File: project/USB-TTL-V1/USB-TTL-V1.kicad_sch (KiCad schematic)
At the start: 22 parts, among them J1 TTL, J2 usbc, Q1 q1, Q2 q2, U1 CH340C, U2 SPX3819M5-L-3-3

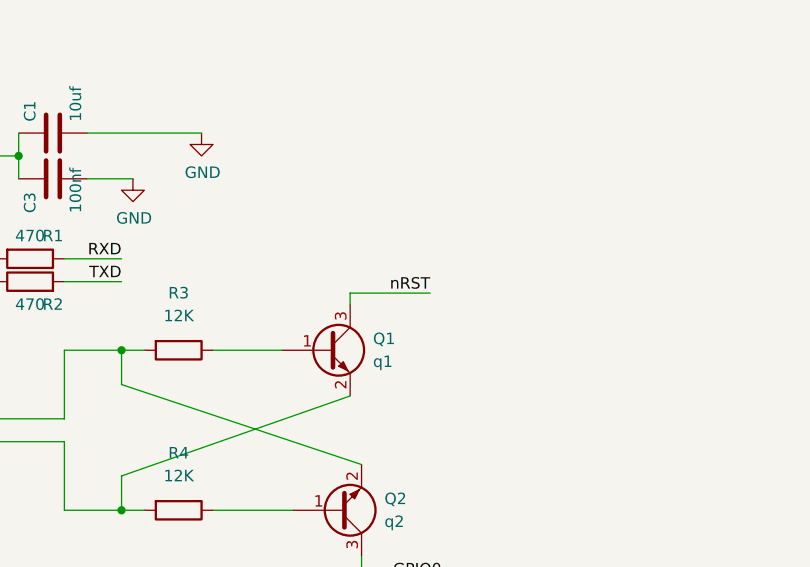
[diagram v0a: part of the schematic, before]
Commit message: fix: screen rst and cs
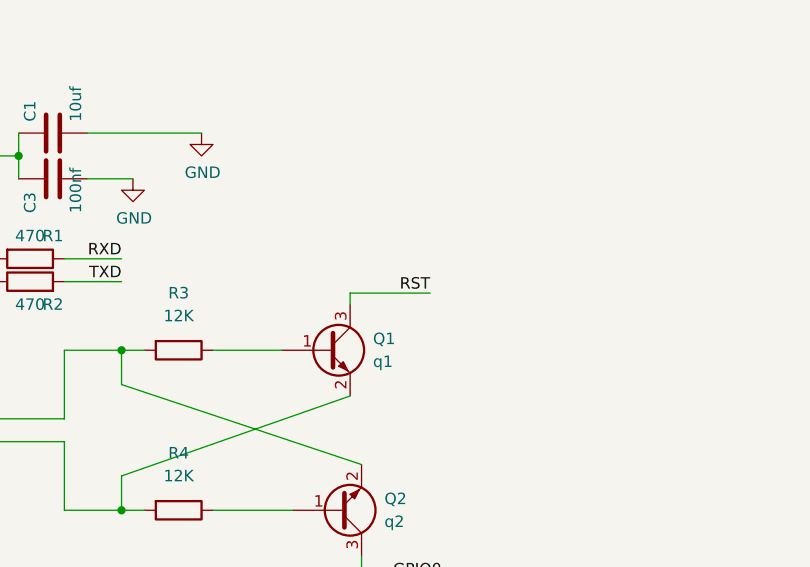
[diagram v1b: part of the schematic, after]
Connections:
- net nRST is gone; now on net RST: Q1.3 (C)
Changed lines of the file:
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@@
     (effects (font (size 4 4) (thickness 0.8) bold) (justify left bottom))
   )
-  (label "nRST" (at 162.56 80.645 180)
+  (label "RST" (at 162.56 80.645 180)
     (effects (font (size 1.27 1.27)) (justify right bottom))
   )
@@
   (symbol (lib_id "power:PWR_FLAG") (at 101.6 102.235 90) (unit 1)
     (in_bom yes) (on_board yes) (fields_autoplaced)
-    (property "Reference" "#FLG03" (id 0) (at 99.695 102.235 0)
+    (property "Reference" "#FLG02" (id 0) (at 99.695 102.235 0)
       (effects (font (size 1.27 1.27)) hide)
     )
@@
     )
     (path "/3b49870e-47e1-4887-b360-7eb0723c5606"
-      (reference "#FLG03") (unit 1) (value "PWR_FLAG") (footprint "")
+      (reference "#FLG02") (unit 1) (value "PWR_FLAG") (footprint "")
     )
     (path "/01c05c7f-9a74-4acc-95cb-f339df8cb185"

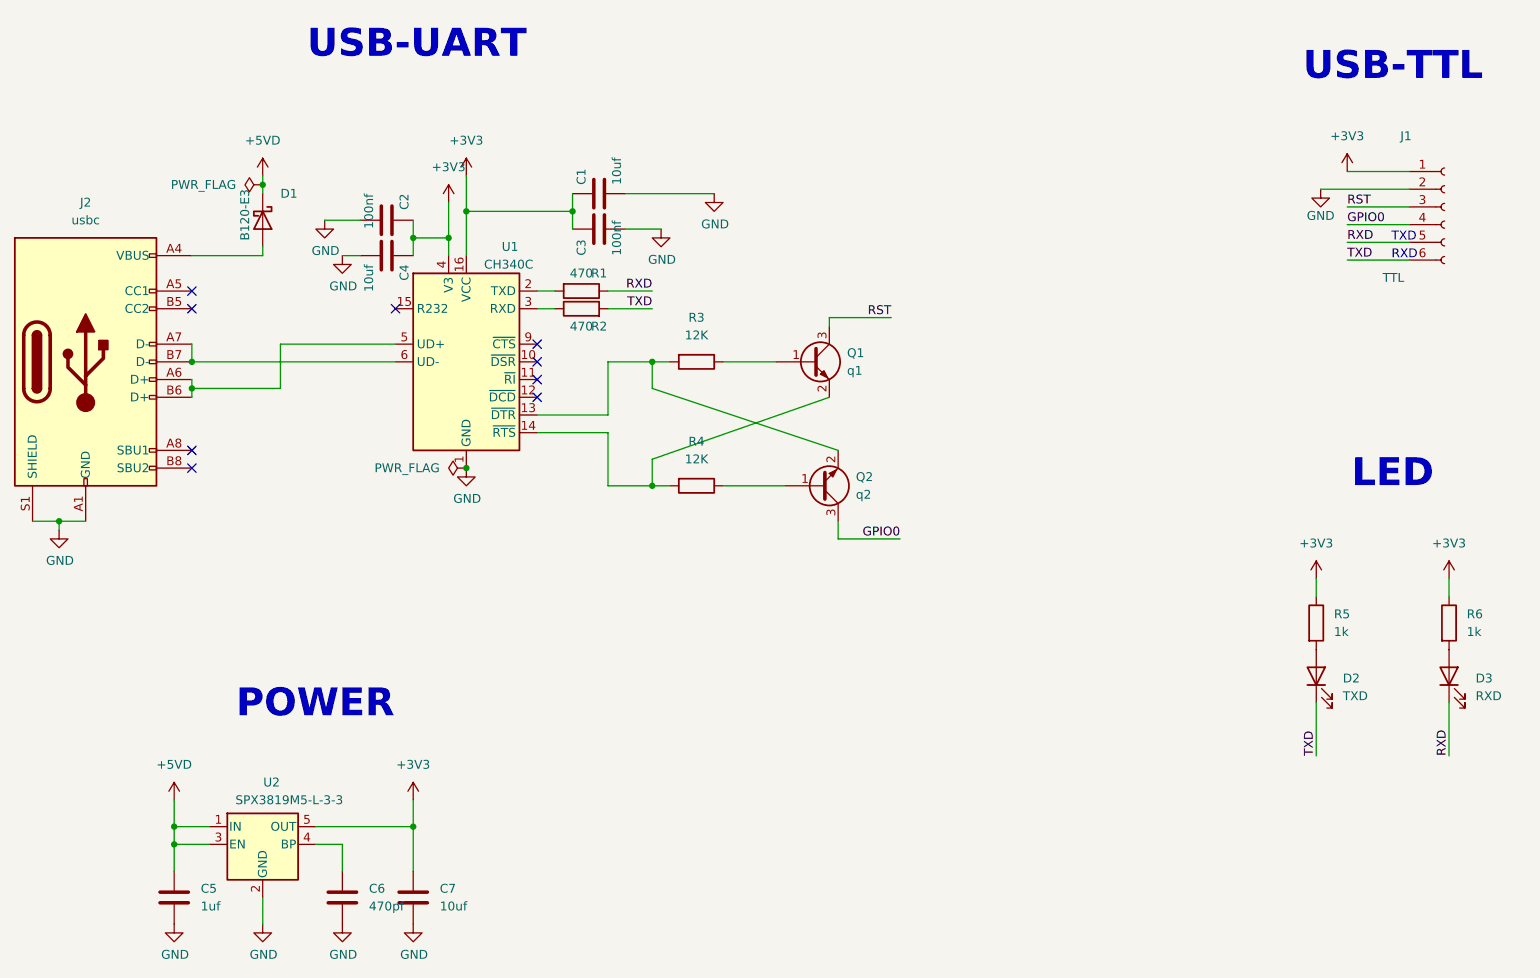
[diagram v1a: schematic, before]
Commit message: feat: update usb - ttl
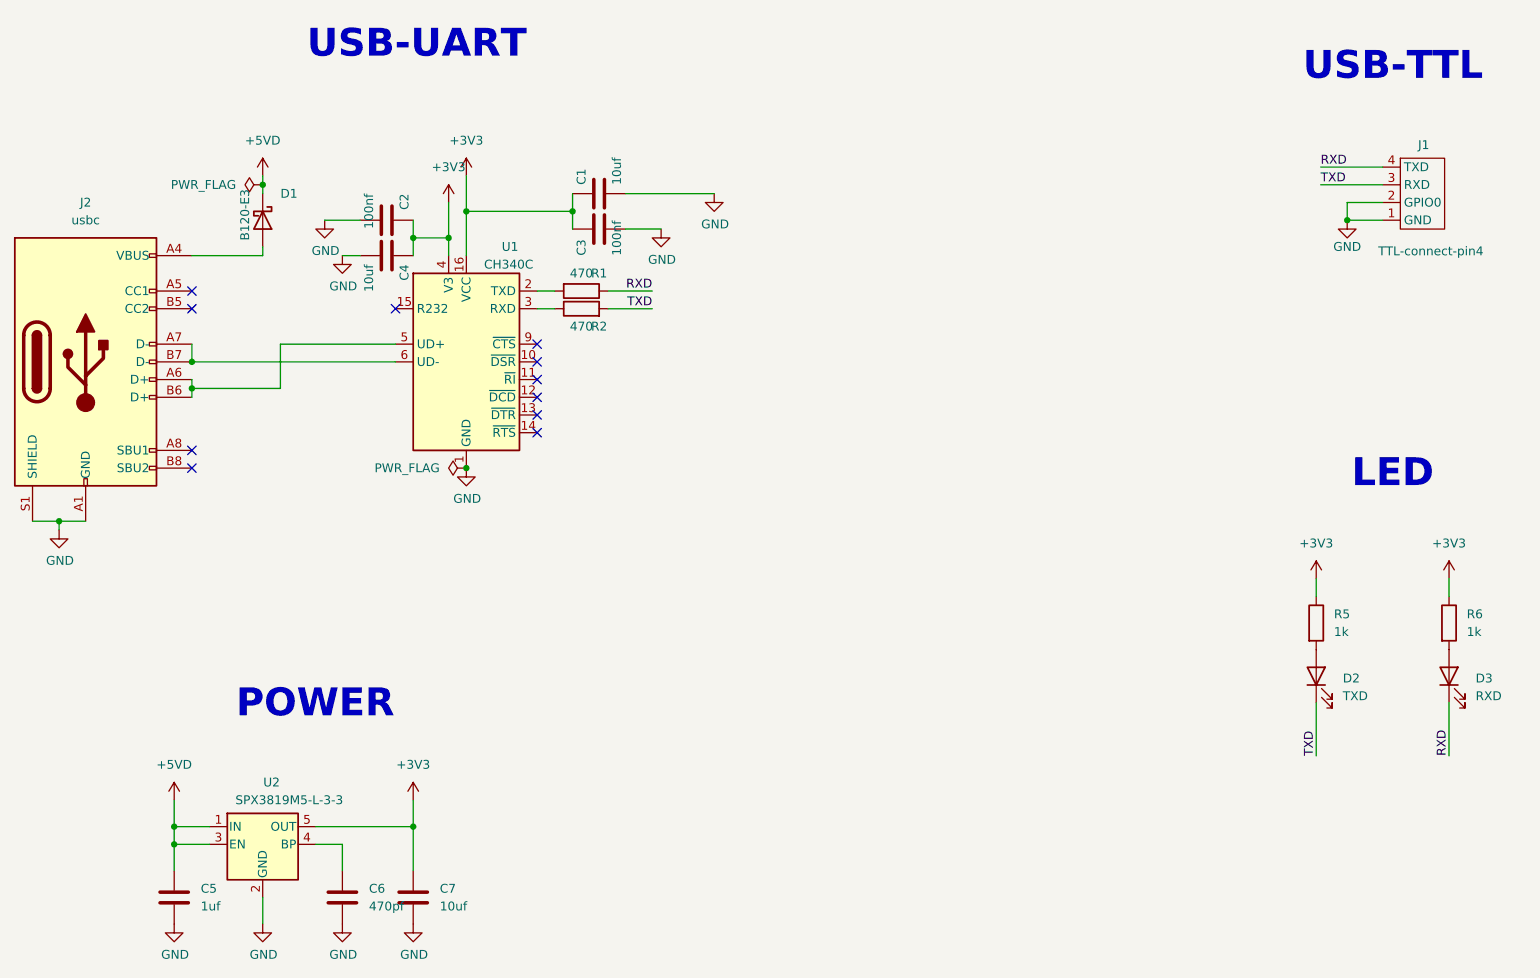
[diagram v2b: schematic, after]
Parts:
- removed J1: TTL, Connector_PinHeader_1.27mm:PinHeader_1x06_P1.27mm_Vertical, symbol Connector:Conn_01x06_Female
- removed Q1: q1, Package_TO_SOT_SMD:TSOT-23, symbol Device:Q_NPN_BEC
- removed Q2: q2, Package_TO_SOT_SMD:TSOT-23, symbol Device:Q_NPN_BEC
- removed R3, R4: 12K, Resistor_SMD:R_0402_1005Metric, symbol Device:R
- added J1: TTL-connect-pin4, Connector_PinHeader_1.27mm:PinHeader_1x04_P1.27mm_Vertical, symbol My-lib:TTL-connect-pin4
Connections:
- net GND: now also J1.1 (GND), J1.2 (GPIO0)
- net RXD: now also J1.4 (TXD)
- net TXD: now also J1.3 (RXD)
- no-connect marks 9 -> 11
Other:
- note removed: "RXD"
- note removed: "TXD"

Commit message: fix: update screen  usb-ttl
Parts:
- removed C4, C7: 10uf, Capacitor_SMD:C_0402_1005Metric, symbol Device:C
- removed C5: 1uf, Capacitor_SMD:C_0402_1005Metric, symbol Device:C
- removed C6: 470pf, Capacitor_SMD:C_0402_1005Metric, symbol Device:C
- removed D1: B120-E3, Diode_SMD:D_SOD-123, symbol Diode:B120-E3
- removed U2: SPX3819M5-L-3-3, Package_TO_SOT_SMD:SOT-23-5, symbol Regulator_Linear:SPX3819M5-L-3-3
- added Q1, Q2: S8050, Package_TO_SOT_SMD:TSOT-23, symbol Device:Q_NPN_BEC
- added R3, R4: 12K, Resistor_SMD:R_0402_1005Metric, symbol Device:R
- J1: footprint Connector_PinHeader_1.27mm:PinHeader_1x04_P1.27mm_Vertical -> Connector_PinHeader_2.00mm:PinHeader_1x05_P2.00mm_Vertical
- R5, R6: value 1k -> 4.7k
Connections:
- net GND: no longer J1.2 (GPIO0)
- net RXD: now also J1.3 (RXD); no longer J1.4 (TXD)
- net TXD: now also J1.4 (TXD); no longer J1.3 (RXD)
- net +5V: now reaches J2.A4 (VBUS), J2.A9 (VBUS), J2.B4 (VBUS), J2.B9 (VBUS)
- net +5V: now also C1.1, C2.1, R5.1, R6.1, U1.16 (VCC)
- net at U1.13 (~{DTR}): now also Q2.2 (E), R3.2
- net at U1.14 (~{RTS}): now also Q1.2 (E), R4.2
- removed net +3V3: C1.1, C2.1, C3.1, R5.1, R6.1, U1.16 (VCC), U1.4 (V3)
- new net: C3.1, U1.4 (V3)
- new net: Q2.1 (B), R4.1
- new net: Q1.1 (B), R3.1
- new net EN: J1.5 (RST), Q1.3 (C)
- new net GPIO0: J1.2 (GPIO0), Q2.3 (C)
- no-connect marks 11 -> 9
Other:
- note removed: "POWER"

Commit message: update
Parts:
- removed R1, R2: 470, Resistor_SMD:R_0402_1005Metric, symbol Device:R
- R5, R6: value 4.7k -> 12K
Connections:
- net RXD: now also U1.2 (TXD)
- net TXD: now also U1.3 (RXD)
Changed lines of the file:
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@@
     (stroke (width 0) (type default) (color 0 0 0 0))
   )
-  (wire (pts (xy 127.635 69.85) (xy 133.985 69.85))
+  (wire (pts (xy 117.475 69.85) (xy 126.365 69.85))
     (stroke (width 0) (type default) (color 0 0 0 0))
   )
@@
     (stroke (width 0) (type default) (color 0 0 0 0))
   )
-  (wire (pts (xy 117.475 72.39) (xy 120.015 72.39))
-    (stroke (width 0) (type default) (color 0 0 0 0))
-  )
   (wire (pts (xy 142.875 55.88) (xy 130.175 55.88))
     (stroke (width 0) (type default) (color 0 0 0 0))
@@
     (stroke (width 0) (type default) (color 0 0 0 0))
   )
-  (wire (pts (xy 127.635 72.39) (xy 133.985 72.39))
+  (wire (pts (xy 117.475 72.39) (xy 126.365 72.39))
     (stroke (width 0) (type default) (color 0 0 0 0))
   )
@@
   )
   (wire (pts (xy 76.2 80.01) (xy 76.2 72.39))
-    (stroke (width 0) (type default) (color 0 0 0 0))
-  )
-  (wire (pts (xy 117.475 69.85) (xy 120.015 69.85))
     (stroke (width 0) (type default) (color 0 0 0 0))
   )
@@
     (effects (font (size 1.27 1.27)) (justify left bottom))
   )
-  (label "TXD" (at 133.985 72.39 180)
+  (label "TXD" (at 126.365 72.39 180)
     (effects (font (size 1.27 1.27)) (justify right bottom))
   )
@@
     (effects (font (size 1.27 1.27)) (justify right bottom))
   )
-  (label "RXD" (at 133.985 69.85 180)
+  (label "RXD" (at 126.365 69.85 180)
     (effects (font (size 1.27 1.27)) (justify right bottom))
   )
@@
     )
     (pin "1")
-  )
-  (symbol (lib_id "Device:R") (at 123.825 69.85 270) (unit 1)
-    (in_bom yes) (on_board yes)
-    (property "Reference" "R1" (id 0) (at 128.27 67.31 90))
-    (property "Value" "470" (id 1) (at 123.825 67.31 90))
-    (property "Footprint" "Resistor_SMD:R_0402_1005Metric" (id 2) (at 123.825 68.072 90)
-      (effects (font (size 1.27 1.27)) hide)
-    )
-    (property "Datasheet" "~" (id 3) (at 123.825 69.85 0)
-      (effects (font (size 1.27 1.27)) hide)
-    )
-    (pin "1")
-    (pin "2")
   )
   (symbol (lib_id "Device:LED") (at 223.52 132.08 90) (unit 1)
@@
       (effects (font (size 1.27 1.27)) (justify left))
     )
-    (property "Value" "4.7k" (id 1) (at 245.11 125.7299 0)
+    (property "Value" "12K" (id 1) (at 245.11 125.7299 0)
       (effects (font (size 1.27 1.27)) (justify left))
     )
@@
       (effects (font (size 1.27 1.27)) (justify left))
     )
-    (property "Value" "4.7k" (id 1) (at 226.06 125.7299 0)
+    (property "Value" "12K" (id 1) (at 226.06 125.7299 0)
       (effects (font (size 1.27 1.27)) (justify left))
     )
@@
     (pin "1")
   )
-  (symbol (lib_id "Device:R") (at 123.825 72.39 90) (unit 1)
-    (in_bom yes) (on_board yes)
-    (property "Reference" "R2" (id 0) (at 128.27 74.93 90))
-    (property "Value" "470" (id 1) (at 123.825 74.93 90))
-    (property "Footprint" "Resistor_SMD:R_0402_1005Metric" (id 2) (at 123.825 74.168 90)
-      (effects (font (size 1.27 1.27)) hide)
-    )
-    (property "Datasheet" "~" (id 3) (at 123.825 72.39 0)
-      (effects (font (size 1.27 1.27)) hide)
-    )
-    (pin "1")
-    (pin "2")
-  )
   (symbol (lib_id "power:GND") (at 48.895 97.79 0) (unit 1)
     (in_bom yes) (on_board yes)
@@
       (reference "Q2") (unit 1) (value "S8050") (footprint "Package_TO_SOT_SMD:TSOT-23")
     )
-    (path "/0c12c629-c4ca-4323-b38e-5b2bbb8af401"
-      (reference "R1") (unit 1) (value "470") (footprint "Resistor_SMD:R_0402_1005Metric")
-    )
-    (path "/e70834ba-5cad-465b-8f2a-fe718c5aad05"
-      (reference "R2") (unit 1) (value "470") (footprint "Resistor_SMD:R_0402_1005Metric")
-    )
     (path "/b4295581-cace-452b-8597-437557d20998"
       (reference "R3") (unit 1) (value "12K") (footprint "Resistor_SMD:R_0402_1005Metric")
@@
     )
     (path "/ca1390ab-054a-4651-ad66-01c546d8e334"
-      (reference "R5") (unit 1) (value "4.7k") (footprint "Resistor_SMD:R_0402_1005Metric")
+      (reference "R5") (unit 1) (value "12K") (footprint "Resistor_SMD:R_0402_1005Metric")
     )
     (path "/4bbcdc80-faa1-4b66-bcc9-8117a3e85f8f"
-      (reference "R6") (unit 1) (value "4.7k") (footprint "Resistor_SMD:R_0402_1005Metric")
+      (reference "R6") (unit 1) (value "12K") (footprint "Resistor_SMD:R_0402_1005Metric")
     )
     (path "/28c1d711-d42c-4ddf-b04a-4befe5087ae7"
